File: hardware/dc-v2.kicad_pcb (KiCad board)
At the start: 2 copper layers, 40 x 40 mm, 43 parts, among them P1 black, P101 CON-SENSOR2, P102 DEBUG, P103 BOOT, P2 green, Q1 FDS8449, U1 MC33926, U101 XMC1XXX, U103 DRILL, U104 DRILL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

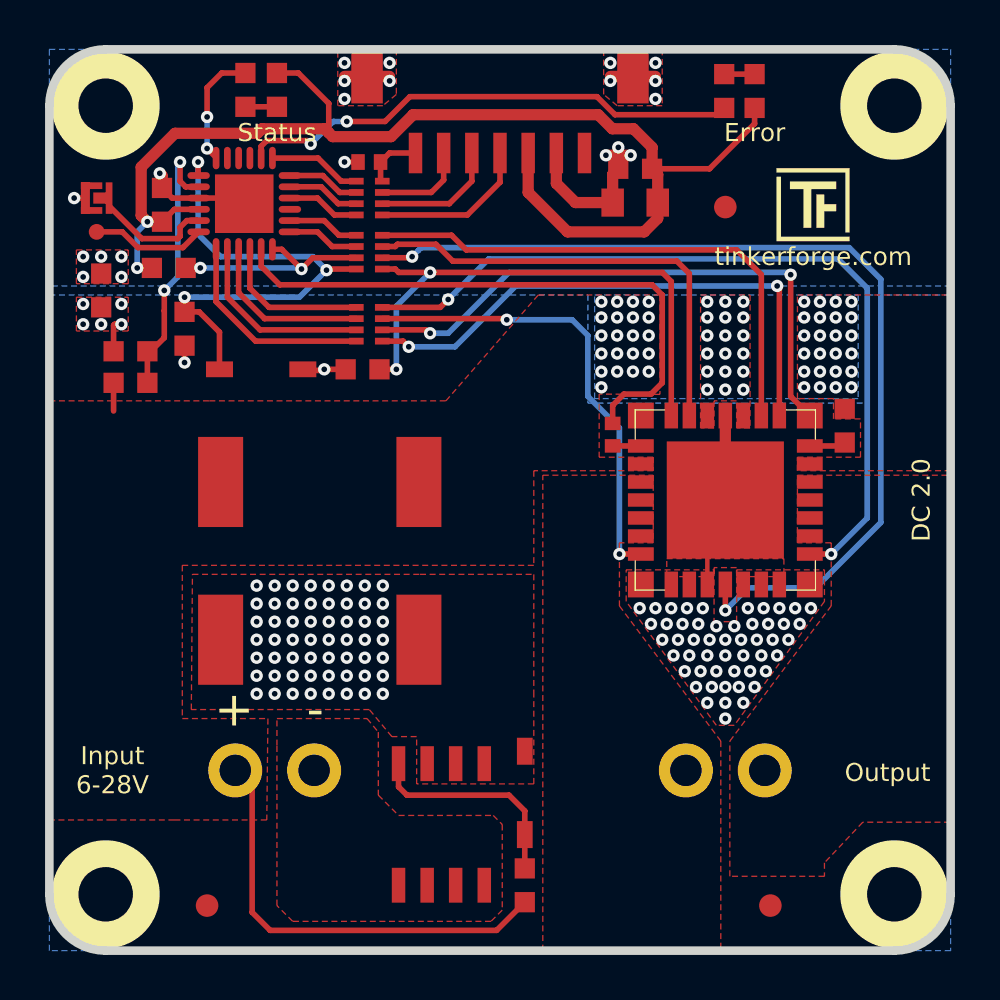
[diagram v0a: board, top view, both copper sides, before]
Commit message: Rev 2.1 : changed Status LED pin, changed footprint R1 to 0603F, added Via's under MC33926 IC
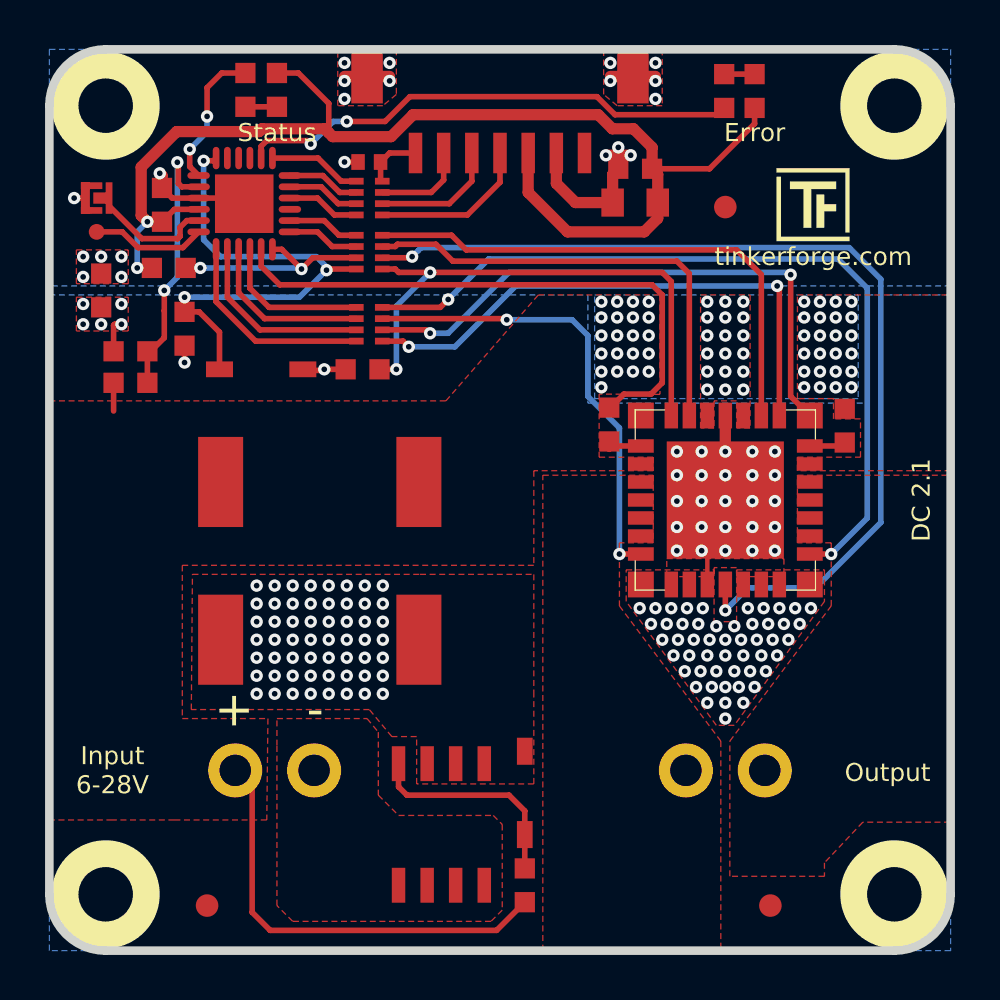
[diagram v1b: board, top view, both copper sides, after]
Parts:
- R1: footprint kicad-libraries:R0402F -> kicad-libraries:R0603F
- moved R1 0.47 mm to (124.8, 116.7)
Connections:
- U101 pad 6: Net-(R101-Pad1) -> PWR-FB
- U101 pad 7: PWR-FB -> Net-(R101-Pad1)
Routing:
- net Net-(R101-Pad1): track 5.26 -> 6.39 mm
- net PWR-EN: track 26.4 -> 25.9 mm
- net AGND: vias 114 -> 139
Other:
- board text added: "DC 2.1"
- board text removed: "DC 2.0"

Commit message: specify processor
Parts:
- U101: value XMC1XXX -> XMC1302
